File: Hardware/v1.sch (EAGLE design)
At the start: 83 parts, among them IC1 LM324D, IC2 m328p, IC3 REG1117, J2 22-27-2031-03, J3 22-27-2021-02, J4 22-27-2031-03, J5 22-27-2041-04, J6 22-27-2071-07, Q1 BSS123, Q2 BSS123, Q3 BSS123, Q5 BSS123

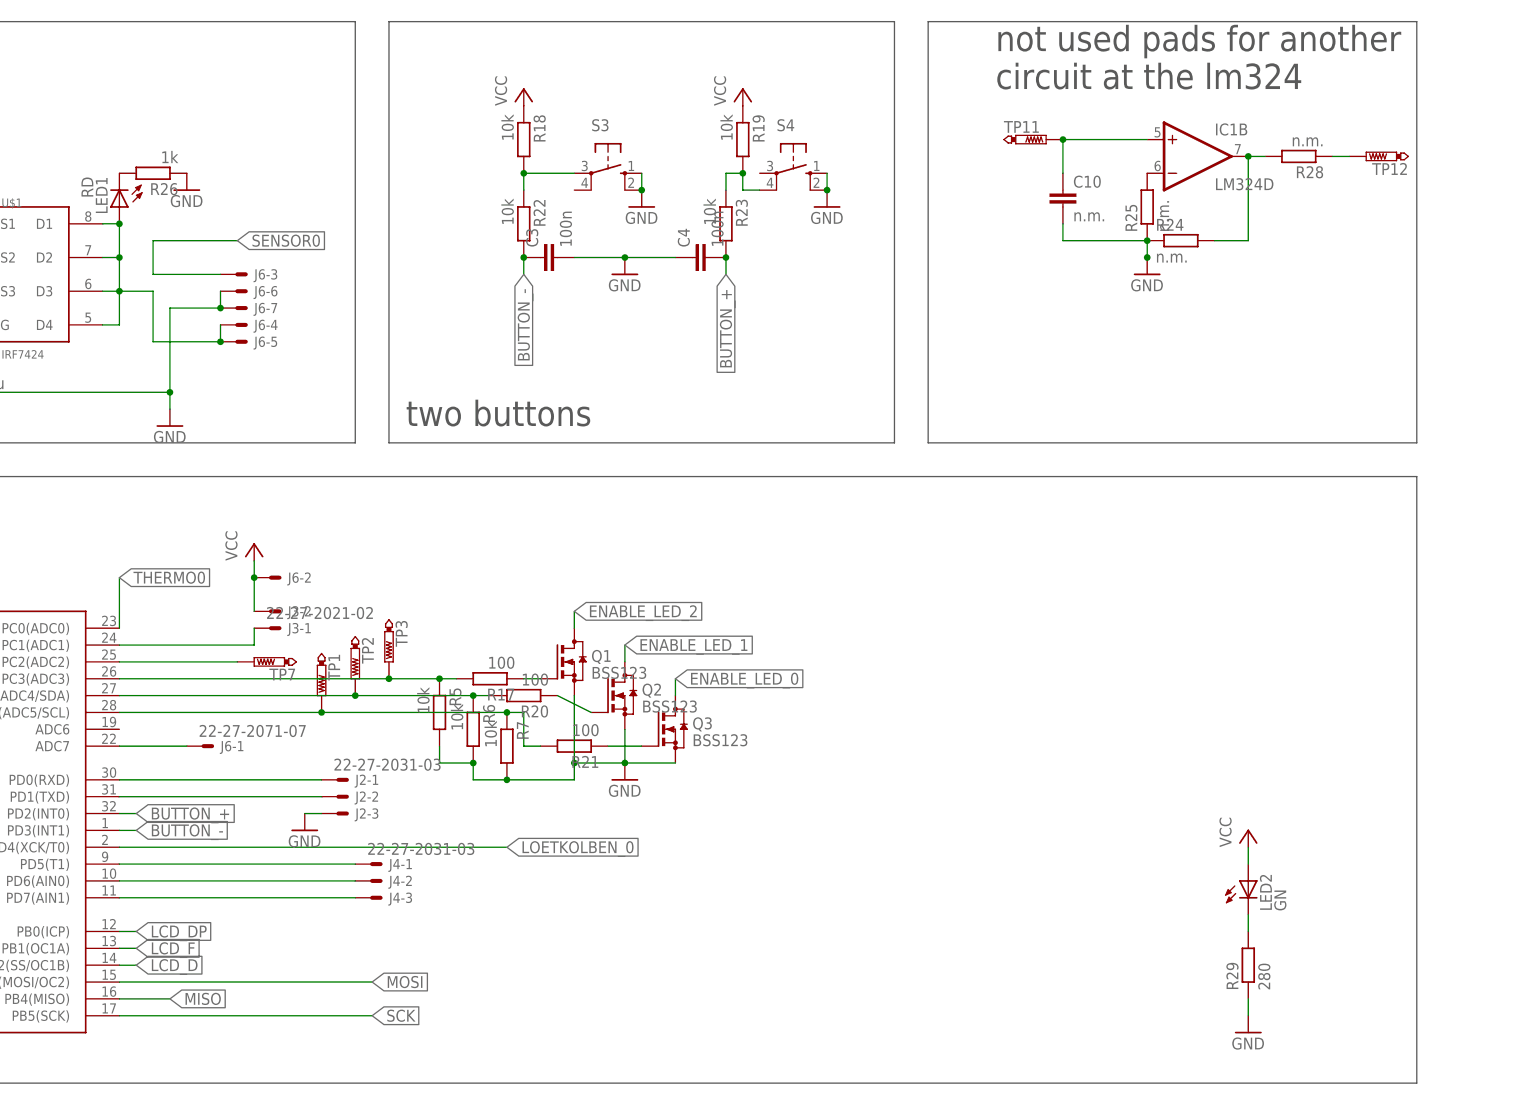
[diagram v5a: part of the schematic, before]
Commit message: all changes described in #64 pull ups are 10k
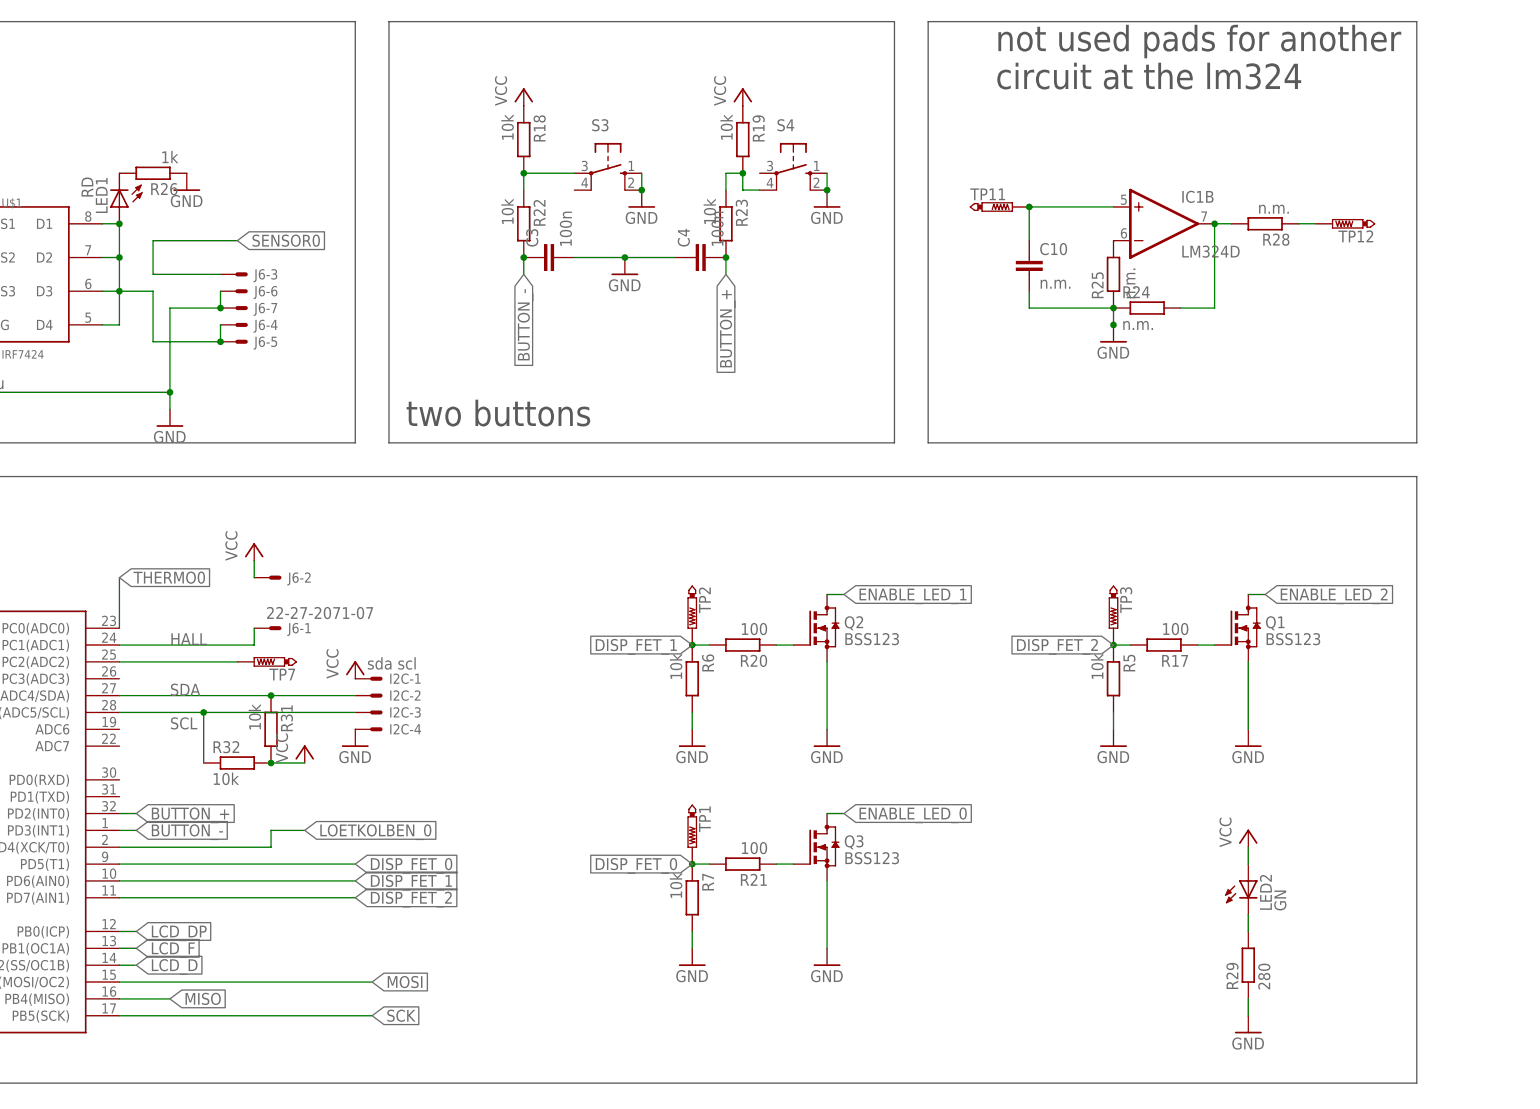
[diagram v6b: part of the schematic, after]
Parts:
- removed J2, J4: 22-27-2031-03, con-molex:22-27-2031-03
- removed J3: 22-27-2021-02, con-molex:22-27-2021-02
- added I2C: sda scl, con-molex:22-27-2041-04
- added R31, R32: 10k, rcl:R-EU_R0603
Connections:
- removed net N$10: IC2.PC4(ADC4/SDA), R20.2, R6.1, TP2.TP
- removed net N$2: IC2.PC3(ADC3), R17.2, R5.1, TP3.TP
- removed net N$28: IC2.PD1(TXD), J2-2.S
- removed net N$29: IC2.PD0(RXD), J2-1.S
- removed net N$4: IC2.PC5(ADC5/SCL), R21.2, R7.1, TP1.TP
- removed net PD5: IC2.PD5(T1), J4-1.S
- removed net PD6: IC2.PD6(AIN0), J4-2.S
- removed net PD7: IC2.PD7(AIN1), J4-3.S
- removed net STH: IC2.PC1(ADC1), J3-1.S
- new net DISP_FET_0: IC2.PD5(T1), R21.2, R7.1, TP1.TP
- new net DISP_FET_1: IC2.PD6(AIN0), R20.2, R6.1, TP2.TP
- new net DISP_FET_2: IC2.PD7(AIN1), R17.2, R5.1, TP3.TP
- new net SCL: I2C-3.S, IC2.PC5(ADC5/SCL), R32.1
- new net SDA: I2C-2.S, IC2.PC4(ADC4/SDA), R31.1
- net GND: now also I2C-4.S; no longer J2-3.S
- net HALL: now also IC2.PC1(ADC1); no longer IC2.ADC7
- net VCC: now also I2C-1.S, R31.2, R32.2; no longer J3-2.S
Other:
- moved on the sheet: C10, IC1B, J6-1, Q1, Q2, Q3, R17, R20, R21, R24, R25, R28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

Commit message: changed schematic (#65)
no real changes
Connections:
- net DISP_FET_0 renamed DISP_ENABLE_0
- net ENABLE_LED_0 renamed DISP_CC_0
- net ENABLE_LED_2 renamed DISP_CC_2
- new net DISP_CC_1: Q2.D
- new net DISP_ENABLE_1: R20.2, R6.1, TP2.TP
- new net DISP_ENABLE_2: R17.2, R5.1, TP3.TP
- net DISP_FET_1: no longer R20.2, R6.1, TP2.TP
- net DISP_FET_2: no longer R17.2, R5.1, TP3.TP
- net ENABLE_LED_1: no longer Q2.D
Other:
- moved on the sheet: Q1, Q2, Q3, R17, R20, R21, R5, R6, R7, TP1, TP2, TP3
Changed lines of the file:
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@@
 <instance part="U$2" gate="G$1" x="226.06" y="43.18"/>
 <instance part="GND5" gate="1" x="76.2" y="218.44"/>
-<instance part="Q1" gate="G$1" x="373.38" y="170.18"/>
-<instance part="Q2" gate="G$1" x="309.88" y="170.18"/>
-<instance part="Q3" gate="G$1" x="309.88" y="137.16"/>
-<instance part="GND10" gate="1" x="309.88" y="152.4"/>
-<instance part="R5" gate="G$1" x="353.06" y="162.56" rot="R270"/>
-<instance part="R6" gate="G$1" x="289.56" y="162.56" rot="R270"/>
-<instance part="R7" gate="G$1" x="289.56" y="129.54" rot="R270"/>
+<instance part="Q1" gate="G$1" x="365.76" y="86.36"/>
+<instance part="Q2" gate="G$1" x="365.76" y="53.34"/>
+<instance part="Q3" gate="G$1" x="302.26" y="53.34"/>
+<instance part="GND10" gate="1" x="365.76" y="35.56"/>
+<instance part="R5" gate="G$1" x="345.44" y="78.74" rot="R270"/>
+<instance part="R6" gate="G$1" x="345.44" y="45.72" rot="R270"/>
+<instance part="R7" gate="G$1" x="281.94" y="45.72" rot="R270"/>
 <instance part="C15" gate="G$1" x="83.82" y="195.58"/>
-<instance part="TP1" gate="G$1" x="289.56" y="137.16" rot="R180"/>
-<instance part="TP2" gate="G$1" x="289.56" y="170.18" rot="R180"/>
-<instance part="TP3" gate="G$1" x="353.06" y="170.18" rot="R180"/>
+<instance part="TP1" gate="G$1" x="281.94" y="53.34" rot="R180"/>
+<instance part="TP2" gate="G$1" x="345.44" y="53.34" rot="R180"/>
+<instance part="TP3" gate="G$1" x="345.44" y="86.36" rot="R180"/>
 <instance part="TP4" gate="G$1" x="50.8" y="76.2" rot="R90"/>
 <instance part="TP5" gate="G$1" x="134.62" y="213.36" rot="R180"/>
@@
 <instance part="R14" gate="G$1" x="248.92" y="68.58" rot="R90"/>
 <instance part="R15" gate="G$1" x="167.64" y="220.98" rot="R180"/>
-<instance part="R17" gate="G$1" x="360.68" y="167.64" rot="R180"/>
-<instance part="R20" gate="G$1" x="297.18" y="167.64" rot="R180"/>
+<instance part="R17" gate="G$1" x="353.06" y="83.82" rot="R180"/>
+<instance part="R20" gate="G$1" x="353.06" y="50.8" rot="R180"/>
 <instance part="R16" gate="G$1" x="144.78" y="210.82" rot="R180"/>
-<instance part="R21" gate="G$1" x="297.18" y="134.62" rot="R180"/>
+<instance part="R21" gate="G$1" x="289.56" y="50.8" rot="R180"/>
 <instance part="R22" gate="G$1" x="264.16" y="231.14" rot="R270"/>
 <instance part="R23" gate="G$1" x="294.64" y="231.14" rot="R270"/>
@@
 <instance part="J6" gate="-7" x="220.98" y="218.44"/>
 <instance part="J6" gate="-5" x="220.98" y="213.36"/>
-<instance part="GND21" gate="1" x="289.56" y="152.4"/>
-<instance part="GND22" gate="1" x="309.88" y="119.38"/>
-<instance part="GND23" gate="1" x="373.38" y="152.4"/>
-<instance part="GND24" gate="1" x="289.56" y="119.38"/>
-<instance part="GND25" gate="1" x="353.06" y="152.4"/>
+<instance part="GND21" gate="1" x="345.44" y="35.56"/>
+<instance part="GND22" gate="1" x="302.26" y="35.56"/>
+<instance part="GND23" gate="1" x="365.76" y="68.58"/>
+<instance part="GND24" gate="1" x="281.94" y="35.56"/>
+<instance part="GND25" gate="1" x="345.44" y="68.58"/>
 <instance part="I2C" gate="-1" x="241.3" y="162.56"/>
 <instance part="I2C" gate="-2" x="241.3" y="160.02"/>
@@
 <pinref part="R6" gate="G$1" pin="2"/>
 <pinref part="GND21" gate="1" pin="GND"/>
-<wire x1="289.56" y1="154.94" x2="289.56" y2="157.48" width="0.1524" layer="91"/>
+<wire x1="345.44" y1="38.1" x2="345.44" y2="40.64" width="0.1524" layer="91"/>
 </segment>
 <segment>
 <pinref part="Q2" gate="G$1" pin="S"/>
-<wire x1="309.88" y1="165.1" x2="309.88" y2="154.94" width="0.1524" layer="91"/>
+<wire x1="365.76" y1="48.26" x2="365.76" y2="38.1" width="0.1524" layer="91"/>
 <pinref part="GND10" gate="1" pin="GND"/>
 </segment>
@@
 <pinref part="Q3" gate="G$1" pin="S"/>
 <pinref part="GND22" gate="1" pin="GND"/>
-<wire x1="309.88" y1="132.08" x2="309.88" y2="121.92" width="0.1524" layer="91"/>
+<wire x1="302.26" y1="48.26" x2="302.26" y2="38.1" width="0.1524" layer="91"/>
 </segment>
 <segment>
 <pinref part="Q1" gate="G$1" pin="S"/>
 <pinref part="GND23" gate="1" pin="GND"/>
-<wire x1="373.38" y1="154.94" x2="373.38" y2="165.1" width="0.1524" layer="91"/>
+<wire x1="365.76" y1="71.12" x2="365.76" y2="81.28" width="0.1524" layer="91"/>
 </segment>
 <segment>
 <pinref part="R7" gate="G$1" pin="2"/>
 <pinref part="GND24" gate="1" pin="GND"/>
-<wire x1="289.56" y1="121.92" x2="289.56" y2="124.46" width="0.1524" layer="91"/>
+<wire x1="281.94" y1="38.1" x2="281.94" y2="40.64" width="0.1524" layer="91"/>
 </segment>
 <segment>
 <pinref part="R5" gate="G$1" pin="2"/>
-<wire x1="353.06" y1="157.48" x2="353.06" y2="154.94" width="0.1524" layer="91"/>
+<wire x1="345.44" y1="73.66" x2="345.44" y2="71.12" width="0.1524" layer="91"/>
 <pinref part="GND25" gate="1" pin="GND"/>
 </segment>
@@
 <label x="182.88" y="45.72" size="1.778" layer="95" rot="R180" xref="yes"/>
 </segment>
-<segment>
-<pinref part="Q2" gate="G$1" pin="D"/>
-<wire x1="312.42" y1="175.26" x2="309.88" y2="175.26" width="0.1524" layer="91"/>
-<label x="312.42" y="175.26" size="1.778" layer="95" xref="yes"/>
-</segment>
-</net>
-<net name="ENABLE_LED_2" class="0">
+</net>
+<net name="DISP_CC_2" class="0">
 <segment>
 <pinref part="U$2" gate="G$1" pin="C3"/>
@@
 <segment>
 <pinref part="Q1" gate="G$1" pin="D"/>
-<wire x1="375.92" y1="175.26" x2="373.38" y2="175.26" width="0.1524" layer="91"/>
-<label x="375.92" y="175.26" size="1.778" layer="95" xref="yes"/>
-</segment>
-</net>
-<net name="ENABLE_LED_0" class="0">
+<wire x1="368.3" y1="91.44" x2="365.76" y2="91.44" width="0.1524" layer="91"/>
+<label x="368.3" y="91.44" size="1.778" layer="95" xref="yes"/>
+</segment>
+</net>
+<net name="DISP_CC_0" class="0">
 <segment>
 <pinref part="U$2" gate="G$1" pin="C1"/>
@@
 <segment>
 <pinref part="Q3" gate="G$1" pin="D"/>
-<wire x1="312.42" y1="142.24" x2="309.88" y2="142.24" width="0.1524" layer="91"/>
-<label x="312.42" y="142.24" size="1.778" layer="95" xref="yes"/>
+<wire x1="304.8" y1="58.42" x2="302.26" y2="58.42" width="0.1524" layer="91"/>
+<label x="304.8" y="58.42" size="1.778" layer="95" xref="yes"/>
 </segment>
 </net>
@@
 </segment>
 </net>
-<net name="DISP_FET_0" class="0">
+<net name="DISP_ENABLE_0" class="0">
 <segment>
 <pinref part="R7" gate="G$1" pin="1"/>
-<wire x1="289.56" y1="134.62" x2="292.1" y2="134.62" width="0.1524" layer="91"/>
-<junction x="289.56" y="134.62"/>
+<wire x1="281.94" y1="50.8" x2="284.48" y2="50.8" width="0.1524" layer="91"/>
+<junction x="281.94" y="50.8"/>
 <pinref part="TP1" gate="G$1" pin="TP"/>
 <pinref part="R21" gate="G$1" pin="2"/>
-<label x="289.56" y="134.62" size="1.778" layer="95" rot="R180" xref="yes"/>
+<label x="281.94" y="50.8" size="1.778" layer="95" rot="R180" xref="yes"/>
 </segment>
 <segment>
@@
 <net name="DISP_FET_1" class="0">
 <segment>
-<pinref part="R6" gate="G$1" pin="1"/>
-<wire x1="292.1" y1="167.64" x2="289.56" y2="167.64" width="0.1524" layer="91"/>
-<junction x="289.56" y="167.64"/>
-<pinref part="TP2" gate="G$1" pin="TP"/>
-<pinref part="R20" gate="G$1" pin="2"/>
-<label x="289.56" y="167.64" size="1.778" layer="95" rot="R180" xref="yes"/>
-</segment>
-<segment>
 <pinref part="IC2" gate="G$1" pin="PD6(AIN0)"/>
 <wire x1="238.76" y1="132.08" x2="203.2" y2="132.08" width="0.1524" layer="91"/>
@@
 </net>
 <net name="DISP_FET_2" class="0">
-<segment>
-<pinref part="R5" gate="G$1" pin="1"/>
-<wire x1="353.06" y1="167.64" x2="355.6" y2="167.64" width="0.1524" layer="91"/>
-<junction x="353.06" y="167.64"/>
-<pinref part="TP3" gate="G$1" pin="TP"/>
-<pinref part="R17" gate="G$1" pin="2"/>
-<label x="353.06" y="167.64" size="1.778" layer="95" rot="R180" xref="yes"/>
-</segment>
 <segment>
 <pinref part="IC2" gate="G$1" pin="PD7(AIN1)"/>
@@
 <pinref part="Q2" gate="G$1" pin="G"/>
 <pinref part="R20" gate="G$1" pin="1"/>
-<wire x1="302.26" y1="167.64" x2="304.8" y2="167.64" width="0.1524" layer="91"/>
+<wire x1="358.14" y1="50.8" x2="360.68" y2="50.8" width="0.1524" layer="91"/>
 </segment>
 </net>
@@
 <segment>
 <pinref part="Q1" gate="G$1" pin="G"/>
-<wire x1="365.76" y1="167.64" x2="368.3" y2="167.64" width="0.1524" layer="91"/>
+<wire x1="358.14" y1="83.82" x2="360.68" y2="83.82" width="0.1524" layer="91"/>
 <pinref part="R17" gate="G$1" pin="1"/>
 </segment>
@@
 <segment>
 <pinref part="Q3" gate="G$1" pin="G"/>
-<wire x1="302.26" y1="134.62" x2="304.8" y2="134.62" width="0.1524" layer="91"/>
+<wire x1="294.64" y1="50.8" x2="297.18" y2="50.8" width="0.1524" layer="91"/>
 <pinref part="R21" gate="G$1" pin="1"/>
 </segment>
@@
 </segment>
 </net>
+<net name="DISP_CC_1" class="0">
+<segment>
+<pinref part="Q2" gate="G$1" pin="D"/>
+<wire x1="368.3" y1="58.42" x2="365.76" y2="58.42" width="0.1524" layer="91"/>
+<label x="368.3" y="58.42" size="1.778" layer="95" xref="yes"/>
+</segment>
+</net>
+<net name="DISP_ENABLE_1" class="0">
+<segment>
+<pinref part="R6" gate="G$1" pin="1"/>
+<wire x1="347.98" y1="50.8" x2="345.44" y2="50.8" width="0.1524" layer="91"/>
+<junction x="345.44" y="50.8"/>
+<pinref part="TP2" gate="G$1" pin="TP"/>
+<pinref part="R20" gate="G$1" pin="2"/>
+<label x="345.44" y="50.8" size="1.778" layer="95" rot="R180" xref="yes"/>
+</segment>
+</net>
+<net name="DISP_ENABLE_2" class="0">
+<segment>
+<pinref part="R5" gate="G$1" pin="1"/>
+<wire x1="345.44" y1="83.82" x2="347.98" y2="83.82" width="0.1524" layer="91"/>
+<junction x="345.44" y="83.82"/>
+<pinref part="TP3" gate="G$1" pin="TP"/>
+<pinref part="R17" gate="G$1" pin="2"/>
+<label x="345.44" y="83.82" size="1.778" layer="95" rot="R180" xref="yes"/>
+</segment>
+</net>

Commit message: something .. i dont know ?!
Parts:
- removed TP11, TP12, TP7: PTR1B1,27, testpad:PTR1B1,27
- added D4: (no value), diode:DIODE-DO214AC
- added J1: UART, con-molex:22-27-2031-03
- added Q4: BSS123, transistor-small-signal:BSS123
- added R33: 330k, rcl:R-EU_R0603
- added R34: 20k, rcl:R-EU_R0603
- added R35, R38, R42: 100k, rcl:R-EU_R0603
- added R39: 68k, rcl:R-EU_R0603
- added R40: 220k, rcl:R-EU_R0603
- added R41: 200k, rcl:R-EU_R0603
- added R43: 11k, rcl:R-EU_R0603
- added R44: 6.2k, rcl:R-EU_R0603
- C10: value n.m. -> 1u; device rcl:C-EUC0603 -> rcl:C-EUC0805
- IC1: value LM324D -> TS914I
- R1: value 43k -> 430k
- R16, R2: value 100 -> 1k
- R24: value n.m. -> 10k
- R25: value n.m. -> 100
- R28: value n.m. -> 1k
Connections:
- net SDFGHJK renamed THERMO0_RAW
- removed net DISP_FET_1: IC2.PD6(AIN0)
- removed net DISP_FET_2: IC2.PD7(AIN1)
- removed net ENABLE_LED_1: U$2.C2
- removed net N$30: C10.1, IC1B.+IN, TP11.TP
- new net ADC3: IC2.PC3(ADC3)
- new net N$10: Q4.G, R24.1, R25.1
- new net N$2: IC2.PD1(TXD), J1-3.S
- new net N$28: R42.1, R43.1, R44.2
- new net N$29: IC1D.OUT, R25.2, R41.2
- new net N$4: IC2.PD0(RXD), J1-2.S
- new net SAFETY: Q4.D, Q5.G, R16.1
- new net THERMO_COARSE: IC1B.OUT, R33.2, R34.1
- new net THERMO_COARSE_INV: D4.A, IC1C.OUT, R35.2
- new net THERMO_VOLTAGE: C10.1, D4.C, IC1D.-IN, R40.2
- net ADC2: no longer TP7.TP
- net DISP_CC_1: now also U$2.C2
- net DISP_ENABLE_1: now also IC2.PD6(AIN0)
- net DISP_ENABLE_2: now also IC2.PD7(AIN1)
- net GND: now also J1-1.S, Q4.S, R24.2, R28.2, R38.2, R40.1, R44.1; no longer R24.1, R25.1
- net N$16: now also IC1B.-IN, R28.1, R33.1; no longer Q5.G, R16.1
- net N$20: now also IC1C.-IN, R34.2, R35.1; no longer IC1B.-IN, R25.2
- net N$21: now also IC1D.+IN, R41.1, R42.2; no longer R28.1, TP12.TP
- net N$26: now also IC1C.+IN, R38.1, R39.2; no longer IC1B.OUT, R24.2, R28.2
- net SENSOR0: now also IC1B.+IN
- net VCC: now also R39.1, R43.2
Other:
- note added: "safety"
- note removed: "not used pads for another circuit at the lm324"
- moved on the sheet: C10, IC1B, LED2, R24, R25, R28, R29
